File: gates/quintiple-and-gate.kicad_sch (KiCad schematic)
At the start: 0 parts

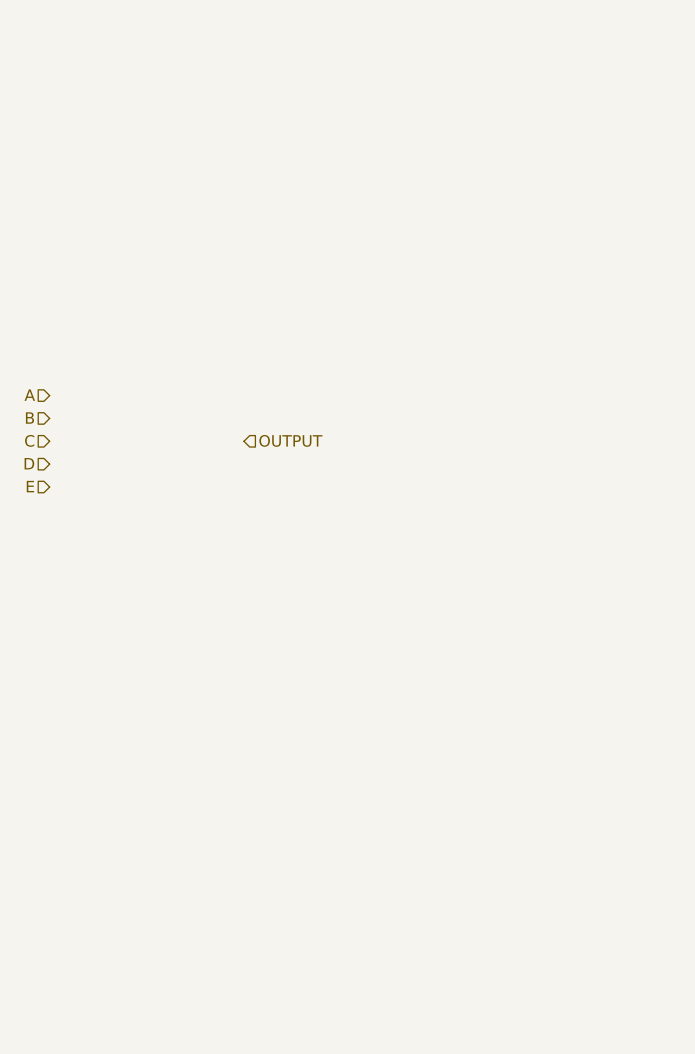
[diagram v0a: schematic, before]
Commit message: Alternative and gates with different amounts of inputs
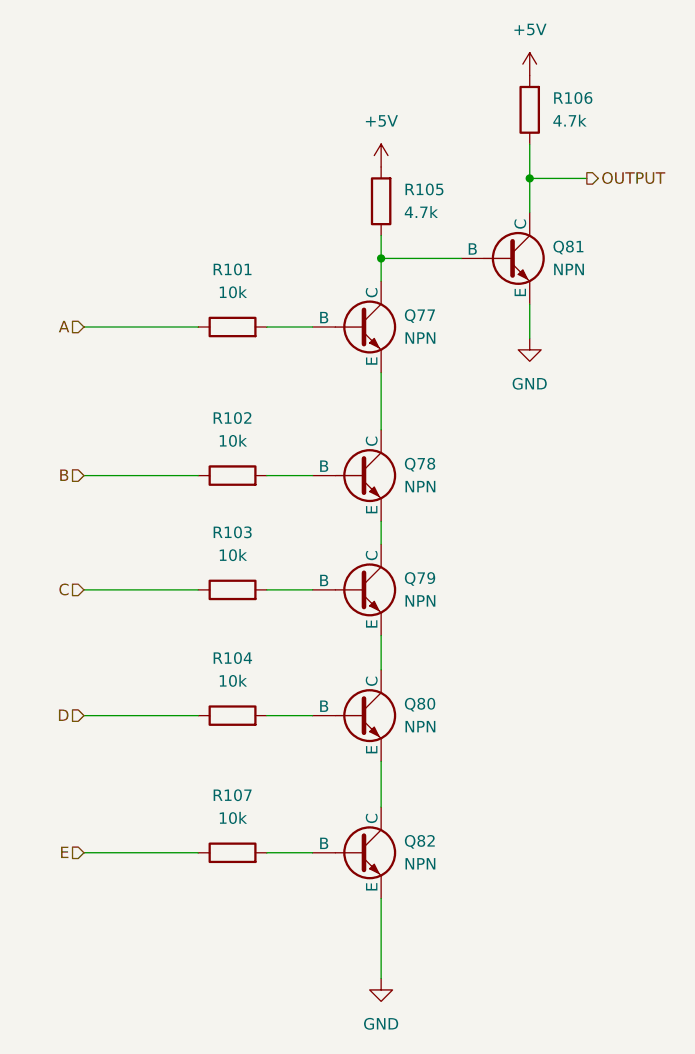
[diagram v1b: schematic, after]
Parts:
- added Q77, Q78, Q79, Q80, Q81, Q82: NPN, SOT-23-3_L2.9-W1.6-P1.90-LS2.8-BR:SOT-23-3_L2.9-W1.6-P1.90-LS2.8-BR, symbol Simulation_SPICE:NPN
- added R101, R102, R103, R104, R107: 10k, R0603:R0603, symbol Device:R
- added R105, R106: 4.7k, R0603:R0603, symbol Device:R
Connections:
- net A: now also R101.1
- net B: now also R102.1
- net C: now also R103.1
- net D: now also R104.1
- net E: now also R107.1
- net OUTPUT: now also Q81.1 (C), R106.1
- new net: Q78.3 (E), Q79.1 (C)
- new net: Q79.2 (B), R103.2
- new net: Q79.3 (E), Q80.1 (C)
- new net: Q80.2 (B), R104.2
- new net: Q77.1 (C), Q81.2 (B), R105.1
- new net: Q78.2 (B), R102.2
- new net: Q80.3 (E), Q82.1 (C)
- new net: Q82.2 (B), R107.2
- new net: Q77.2 (B), R101.2
- new net: Q77.3 (E), Q78.1 (C)
- new net +5V: R105.2, R106.2
- new net GND: Q81.3 (E), Q82.3 (E)

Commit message: complete 2-bit encoder
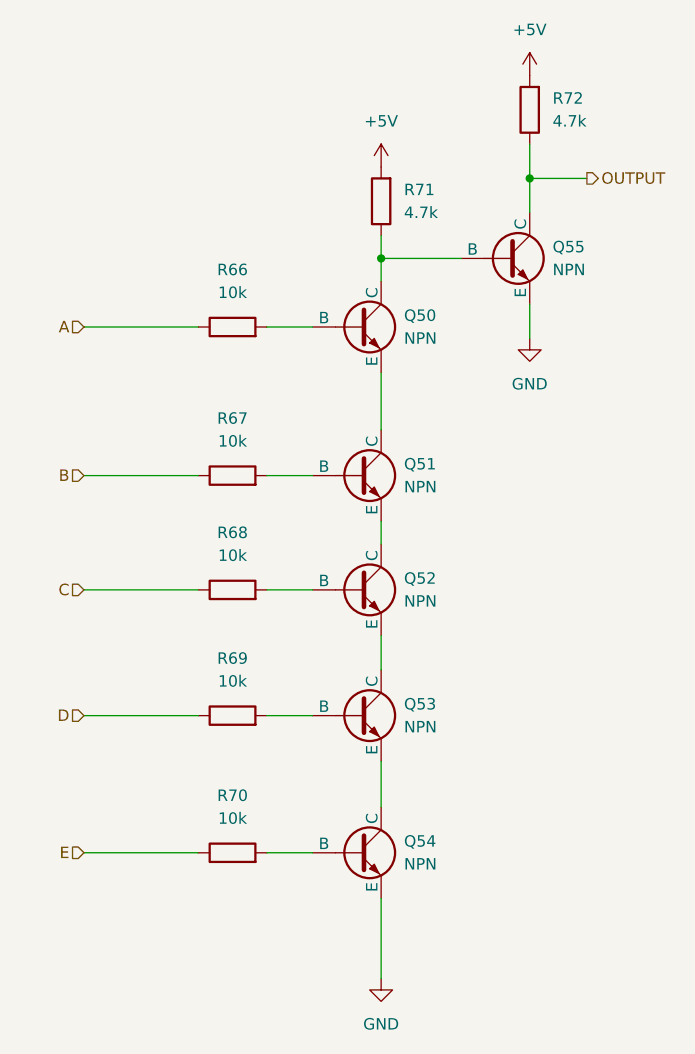
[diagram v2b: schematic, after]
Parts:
- renumbered Q77 to Q50, Q78 to Q51, Q79 to Q52, Q80 to Q53, Q82 to Q54, Q81 to Q55, R101 to R66, R102 to R67, R103 to R68, R104 to R69, R107 to R70, R105 to R71, R106 to R72
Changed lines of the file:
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@@
 		(dnp no)
 		(fields_autoplaced yes)
-		(property "Reference" "Q79"
+		(property "Reference" "Q52"
 			(at 120.65 81.2799 0)
 			(effects
@@
 			(project "control-unit"
 				(path "/1cf3a7ee-ec47-45b6-b515-1840d726ab8f/0fc48953-2111-4879-91f3-de7a19ca0ce9"
-					(reference "Q79")
+					(reference "Q52")
 					(unit 1)
 				)
@@
 		(dnp no)
 		(fields_autoplaced yes)
-		(property "Reference" "#PWR091"
+		(property "Reference" "#PWR066"
 			(at 134.62 29.21 0)
 			(effects
@@
 			)
 		)
-		(property "Description" ""
+		(property "Description" "Power symbol creates a global label with name \"+5V\""
 			(at 134.62 25.4 0)
 			(effects
@@
 			(project "control-unit"
 				(path "/1cf3a7ee-ec47-45b6-b515-1840d726ab8f/0fc48953-2111-4879-91f3-de7a19ca0ce9"
-					(reference "#PWR091")
+					(reference "#PWR066")
 					(unit 1)
 				)
@@
 		(dnp no)
 		(fields_autoplaced yes)
-		(property "Reference" "R106"
+		(property "Reference" "R72"
 			(at 137.16 27.9399 0)
 			(effects
@@
 			(project "control-unit"
 				(path "/1cf3a7ee-ec47-45b6-b515-1840d726ab8f/0fc48953-2111-4879-91f3-de7a19ca0ce9"
-					(reference "R106")
+					(reference "R72")
 					(unit 1)
 				)
@@
 		(dnp no)
 		(fields_autoplaced yes)
-		(property "Reference" "R104"
+		(property "Reference" "R69"
 			(at 101.6 90.17 90)
 			(effects
@@
 			(project "control-unit"
 				(path "/1cf3a7ee-ec47-45b6-b515-1840d726ab8f/0fc48953-2111-4879-91f3-de7a19ca0ce9"
-					(reference "R104")
+					(reference "R69")
 					(unit 1)
 				)
@@
 		(dnp no)
 		(fields_autoplaced yes)
-		(property "Reference" "Q81"
+		(property "Reference" "Q55"
 			(at 137.16 44.4499 0)
 			(effects
@@
 			(project "control-unit"
 				(path "/1cf3a7ee-ec47-45b6-b515-1840d726ab8f/0fc48953-2111-4879-91f3-de7a19ca0ce9"
-					(reference "Q81")
+					(reference "Q55")
 					(unit 1)
 				)
@@
 		(dnp no)
 		(fields_autoplaced yes)
-		(property "Reference" "R102"
+		(property "Reference" "R67"
 			(at 101.6 63.5 90)
 			(effects
@@
 			(project "control-unit"
 				(path "/1cf3a7ee-ec47-45b6-b515-1840d726ab8f/0fc48953-2111-4879-91f3-de7a19ca0ce9"
-					(reference "R102")
+					(reference "R67")
 					(unit 1)
 				)
@@
 		(dnp no)
 		(fields_autoplaced yes)
-		(property "Reference" "#PWR089"
+		(property "Reference" "#PWR064"
 			(at 118.11 39.37 0)
 			(effects
@@
 			)
 		)
-		(property "Description" ""
+		(property "Description" "Power symbol creates a global label with name \"+5V\""
 			(at 118.11 35.56 0)
 			(effects
@@
 			(project "control-unit"
 				(path "/1cf3a7ee-ec47-45b6-b515-1840d726ab8f/0fc48953-2111-4879-91f3-de7a19ca0ce9"
-					(reference "#PWR089")
+					(reference "#PWR064")
 					(unit 1)
 				)
@@
 		(dnp no)
 		(fields_autoplaced yes)
-		(property "Reference" "Q82"
+		(property "Reference" "Q54"
 			(at 120.65 110.4899 0)
 			(effects
@@
 			(project "control-unit"
 				(path "/1cf3a7ee-ec47-45b6-b515-1840d726ab8f/0fc48953-2111-4879-91f3-de7a19ca0ce9"
-					(reference "Q82")
+					(reference "Q54")
 					(unit 1)
 				)
@@
 		(dnp no)
 		(fields_autoplaced yes)
-		(property "Reference" "R101"
+		(property "Reference" "R66"
 			(at 101.6 46.99 90)
 			(effects
@@
 			(project "control-unit"
 				(path "/1cf3a7ee-ec47-45b6-b515-1840d726ab8f/0fc48953-2111-4879-91f3-de7a19ca0ce9"
-					(reference "R101")
+					(reference "R66")
 					(unit 1)
 				)
@@
 		(dnp no)
 		(fields_autoplaced yes)
-		(property "Reference" "R107"
+		(property "Reference" "R70"
 			(at 101.6 105.41 90)
 			(effects
@@
 			(project "control-unit"
 				(path "/1cf3a7ee-ec47-45b6-b515-1840d726ab8f/0fc48953-2111-4879-91f3-de7a19ca0ce9"
-					(reference "R107")
+					(reference "R70")
 					(unit 1)
 				)
@@
 		(dnp no)
 		(fields_autoplaced yes)
-		(property "Reference" "#PWR092"
+		(property "Reference" "#PWR067"
 			(at 134.62 60.96 0)
 			(effects
@@
 			)
 		)
-		(property "Description" ""
+		(property "Description" "Power symbol creates a global label with name \"GND\" , ground"
 			(at 134.62 54.61 0)
 			(effects
@@
 			(project "control-unit"
 				(path "/1cf3a7ee-ec47-45b6-b515-1840d726ab8f/0fc48953-2111-4879-91f3-de7a19ca0ce9"
-					(reference "#PWR092")
+					(reference "#PWR067")
 					(unit 1)
 				)
@@
 		(dnp no)
 		(fields_autoplaced yes)
-		(property "Reference" "Q80"
+		(property "Reference" "Q53"
 			(at 120.65 95.2499 0)
 			(effects
@@
 			(project "control-unit"
 				(path "/1cf3a7ee-ec47-45b6-b515-1840d726ab8f/0fc48953-2111-4879-91f3-de7a19ca0ce9"
-					(reference "Q80")
+					(reference "Q53")
 					(unit 1)
 				)
@@
 		(dnp no)
 		(fields_autoplaced yes)
-		(property "Reference" "Q77"
+		(property "Reference" "Q50"
 			(at 120.65 52.0699 0)
 			(effects
@@
 			(project "control-unit"
 				(path "/1cf3a7ee-ec47-45b6-b515-1840d726ab8f/0fc48953-2111-4879-91f3-de7a19ca0ce9"
-					(reference "Q77")
+					(reference "Q50")
 					(unit 1)
 				)
@@
 		(dnp no)
 		(fields_autoplaced yes)
-		(property "Reference" "R103"
+		(property "Reference" "R68"
 			(at 101.6 76.2 90)
 			(effects
@@
 			(project "control-unit"
 				(path "/1cf3a7ee-ec47-45b6-b515-1840d726ab8f/0fc48953-2111-4879-91f3-de7a19ca0ce9"
-					(reference "R103")
+					(reference "R68")
 					(unit 1)
 				)
@@
 		(dnp no)
 		(fields_autoplaced yes)
-		(property "Reference" "Q78"
+		(property "Reference" "Q51"
 			(at 120.65 68.5799 0)
 			(effects
@@
 			(project "control-unit"
 				(path "/1cf3a7ee-ec47-45b6-b515-1840d726ab8f/0fc48953-2111-4879-91f3-de7a19ca0ce9"
-					(reference "Q78")
+					(reference "Q51")
 					(unit 1)
 				)
@@
 		(dnp no)
 		(fields_autoplaced yes)
-		(property "Reference" "R105"
+		(property "Reference" "R71"
 			(at 120.65 38.0999 0)
 			(effects
@@
 			(project "control-unit"
 				(path "/1cf3a7ee-ec47-45b6-b515-1840d726ab8f/0fc48953-2111-4879-91f3-de7a19ca0ce9"
-					(reference "R105")
+					(reference "R71")
 					(unit 1)
 				)
@@
 		(dnp no)
 		(fields_autoplaced yes)
-		(property "Reference" "#PWR090"
+		(property "Reference" "#PWR065"
 			(at 118.11 132.08 0)
 			(effects
@@
 			)
 		)
-		(property "Description" ""
+		(property "Description" "Power symbol creates a global label with name \"GND\" , ground"
 			(at 118.11 125.73 0)
 			(effects
@@
 			(project "control-unit"
 				(path "/1cf3a7ee-ec47-45b6-b515-1840d726ab8f/0fc48953-2111-4879-91f3-de7a19ca0ce9"
-					(reference "#PWR090")
+					(reference "#PWR065")
 					(unit 1)
 				)
